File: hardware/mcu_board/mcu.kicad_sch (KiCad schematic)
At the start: 21 parts, among them J1 TEMP, J4 DISPLAY, J4 LEDS_IN, J7 RTC, SW1 RESET, SW1 RotaryEncoder_Switch, U1 ESP32-S3-DevKitC, U2 TOP, U3 BOTTOM, U4 COLD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

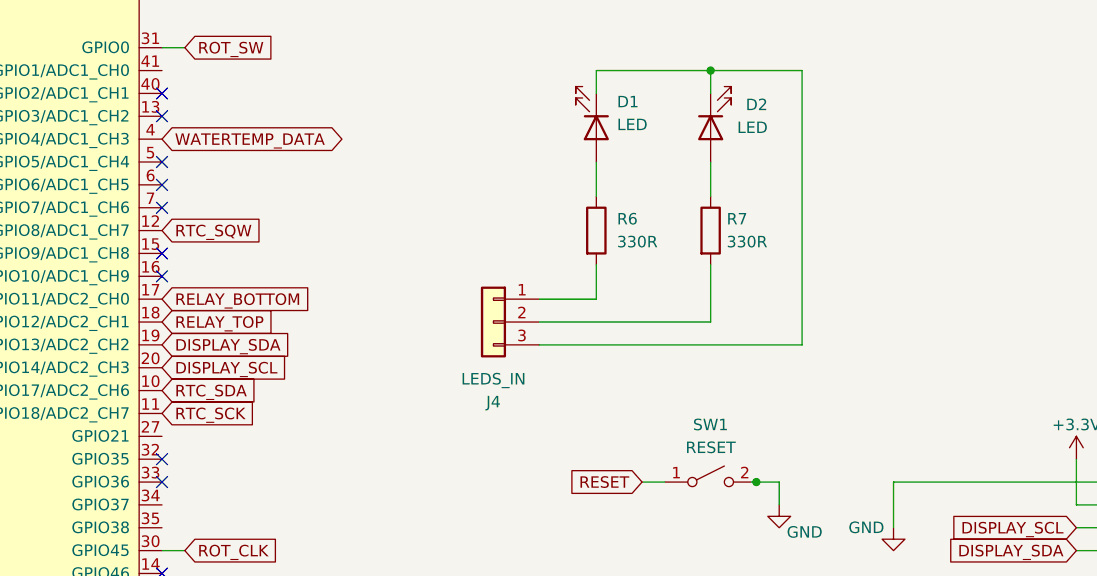
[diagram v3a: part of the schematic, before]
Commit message: fix boards so they components are on the correct side lol
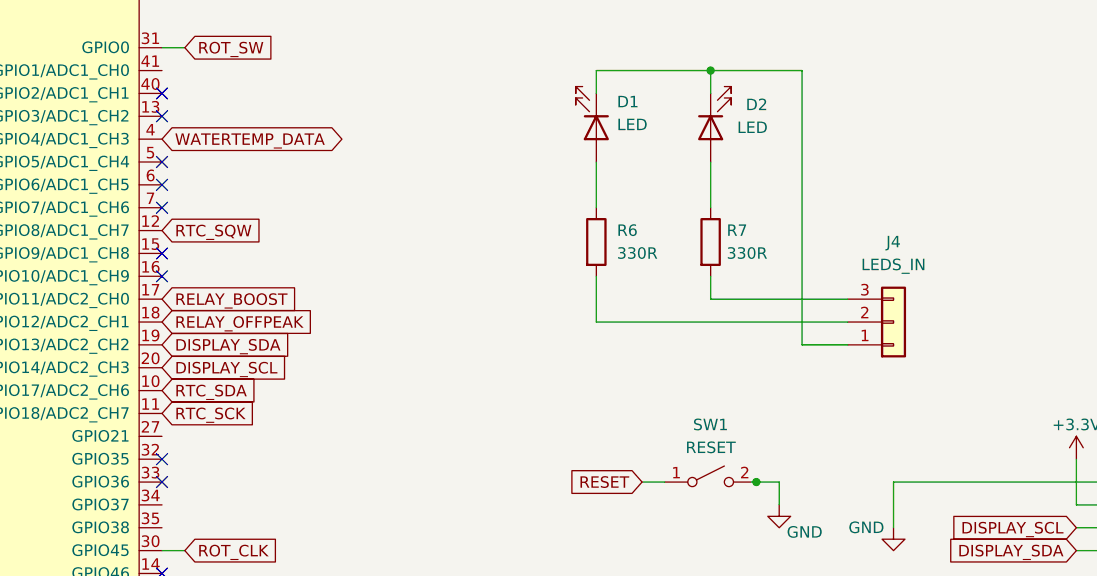
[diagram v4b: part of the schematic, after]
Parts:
- J1: footprint Connector_Audio_2:Jack_3.5mm_PJ320D_Horizontal -> Connector_Audio:Jack_3.5mm_PJ320D_Horizontal
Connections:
- net at D1.1 (K), D2.1 (K): now also J4.1 (Pin_1); no longer J4.3 (Pin_3)
- net at R6.2: now also J4.2 (Pin_2); no longer J4.1 (Pin_1)
- net at R7.2: now also J4.3 (Pin_3); no longer J4.2 (Pin_2)
- net RELAY_BOTTOM renamed RELAY_BOOST
- net RELAY_TOP renamed RELAY_OFFPEAK
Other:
- moved on the sheet: J4, R6, R7
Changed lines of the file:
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@@
+    (stroke (width 0) (type default))
+  )
+  (wire (pts (xy 165.1 81.28) (xy 165.1 83.82))
     (stroke (width 0) (type default))
   )
@@
     (stroke (width 0) (type default))
   )
-  (wire (pts (xy 165.1 68.58) (xy 165.1 72.39))
+  (wire (pts (xy 165.1 68.58) (xy 165.1 73.66))
     (stroke (width 0) (type default))
   )
@@
     (stroke (width 0) (type default))
   )
-  (wire (pts (xy 146.05 88.9) (xy 175.26 88.9))
-    (stroke (width 0) (type default))
-  )
-  (wire (pts (xy 152.4 80.01) (xy 152.4 83.82))
+  (wire (pts (xy 152.4 81.28) (xy 152.4 86.36))
     (stroke (width 0) (type default))
   )
@@
     (stroke (width 0) (type default))
   )
-  (wire (pts (xy 146.05 83.82) (xy 152.4 83.82))
-    (stroke (width 0) (type default))
-  )
   (wire (pts (xy 139.7 40.64) (xy 139.7 43.18))
     (stroke (width 0) (type default))
@@
     (stroke (width 0) (type default))
   )
-  (wire (pts (xy 146.05 86.36) (xy 165.1 86.36))
-    (stroke (width 0) (type default))
-  )
   (wire (pts (xy 205.74 101.6) (xy 205.74 106.68))
     (stroke (width 0) (type default))
@@
     (stroke (width 0) (type default))
   )
+  (wire (pts (xy 165.1 83.82) (xy 180.34 83.82))
+    (stroke (width 0) (type default))
+  )
   (wire (pts (xy 169.672 104.14) (xy 170.18 104.14))
     (stroke (width 0) (type default))
@@
     (stroke (width 0) (type default))
   )
-  (wire (pts (xy 152.4 68.58) (xy 152.4 72.39))
+  (wire (pts (xy 152.4 68.58) (xy 152.4 73.66))
     (stroke (width 0) (type default))
   )
@@
     (stroke (width 0) (type default))
   )
-  (wire (pts (xy 165.1 86.36) (xy 165.1 80.01))
-    (stroke (width 0) (type default))
-  )
   (wire (pts (xy 258.318 65.278) (xy 258.318 61.976))
     (stroke (width 0) (type default))
@@
     (stroke (width 0) (type default))
   )
+  (wire (pts (xy 180.34 86.36) (xy 152.4 86.36))
+    (stroke (width 0) (type default))
+  )
   (wire (pts (xy 262.128 50.546) (xy 253.746 50.546))
     (stroke (width 0) (type default))
@@
   )
   (wire (pts (xy 157.48 137.16) (xy 180.34 137.16))
+    (stroke (width 0) (type default))
+  )
+  (wire (pts (xy 175.26 88.9) (xy 180.34 88.9))
     (stroke (width 0) (type default))
   )
@@
     )
   )
-  (global_label "RELAY_BOTTOM" (shape input) (at 104.14 83.82 0) (fields_autoplaced)
-    (effects (font (size 1.27 1.27)) (justify left))
-    (property "Intersheetrefs" "${INTERSHEET_REFS}" (at 120.9553 83.82 0)
+  (global_label "RELAY_BOOST" (shape input) (at 104.14 83.82 0) (fields_autoplaced)
+    (effects (font (size 1.27 1.27)) (justify left))
+    (property "Intersheetrefs" "${INTERSHEET_REFS}" (at 119.8252 83.82 0)
       (effects (font (size 1.27 1.27)) (justify left) hide)
     )
@@
     )
   )
-  (global_label "RELAY_TOP" (shape input) (at 104.14 86.36 0) (fields_autoplaced)
-    (effects (font (size 1.27 1.27)) (justify left))
-    (property "Intersheetrefs" "${INTERSHEET_REFS}" (at 117.2058 86.36 0)
+  (global_label "RELAY_OFFPEAK" (shape input) (at 104.14 86.36 0) (fields_autoplaced)
+    (effects (font (size 1.27 1.27)) (justify left))
+    (property "Intersheetrefs" "${INTERSHEET_REFS}" (at 122.0024 86.36 0)
       (effects (font (size 1.27 1.27)) (justify left) hide)
     )
@@
       (effects (font (size 1.27 1.27)))
     )
-    (property "Footprint" "Connector_Audio_2:Jack_3.5mm_PJ320D_Horizontal" (at 175.26 33.02 0)
+    (property "Footprint" "Connector_Audio:Jack_3.5mm_PJ320D_Horizontal" (at 175.26 33.02 0)
       (effects (font (size 1.27 1.27)) hide)
     )
@@
     )
   )
-  (symbol (lib_id "Connector_Generic:Conn_01x03") (at 140.97 86.36 0) (mirror y) (unit 1)
-    (in_bom yes) (on_board yes) (dnp no)
-    (property "Reference" "J4" (at 140.97 95.25 0)
-      (effects (font (size 1.27 1.27)))
-    )
-    (property "Value" "LEDS_IN" (at 140.97 92.71 0)
-      (effects (font (size 1.27 1.27)))
-    )
-    (property "Footprint" "Connector_PinHeader_2.54mm:PinHeader_1x03_P2.54mm_Vertical" (at 140.97 86.36 0)
-      (effects (font (size 1.27 1.27)) hide)
-    )
-    (property "Datasheet" "~" (at 140.97 86.36 0)
+  (symbol (lib_id "Connector_Generic:Conn_01x03") (at 185.42 86.36 0) (mirror x) (unit 1)
+    (in_bom yes) (on_board yes) (dnp no)
+    (property "Reference" "J4" (at 185.42 77.47 0)
+      (effects (font (size 1.27 1.27)))
+    )
+    (property "Value" "LEDS_IN" (at 185.42 80.01 0)
+      (effects (font (size 1.27 1.27)))
+    )
+    (property "Footprint" "Connector_PinHeader_2.54mm:PinHeader_1x03_P2.54mm_Vertical" (at 185.42 86.36 0)
+      (effects (font (size 1.27 1.27)) hide)
+    )
+    (property "Datasheet" "~" (at 185.42 86.36 0)
       (effects (font (size 1.27 1.27)) hide)
     )
@@
     )
   )
-  (symbol (lib_id "Device:R") (at 152.4 76.2 0) (unit 1)
+  (symbol (lib_id "Device:R") (at 152.4 77.47 0) (unit 1)
     (in_bom yes) (on_board yes) (dnp no) (fields_autoplaced)
-    (property "Reference" "R6" (at 154.686 74.93 0)
-      (effects (font (size 1.27 1.27)) (justify left))
-    )
-    (property "Value" "330R" (at 154.686 77.47 0)
-      (effects (font (size 1.27 1.27)) (justify left))
-    )
-    (property "Footprint" "Resistor_SMD:R_0805_2012Metric_Pad1.20x1.40mm_HandSolder" (at 150.622 76.2 90)
-      (effects (font (size 1.27 1.27)) hide)
-    )
-    (property "Datasheet" "~" (at 152.4 76.2 0)
+    (property "Reference" "R6" (at 154.686 76.2 0)
+      (effects (font (size 1.27 1.27)) (justify left))
+    )
+    (property "Value" "330R" (at 154.686 78.74 0)
+      (effects (font (size 1.27 1.27)) (justify left))
+    )
+    (property "Footprint" "Resistor_SMD:R_0805_2012Metric_Pad1.20x1.40mm_HandSolder" (at 150.622 77.47 90)
+      (effects (font (size 1.27 1.27)) hide)
+    )
+    (property "Datasheet" "~" (at 152.4 77.47 0)
       (effects (font (size 1.27 1.27)) hide)
     )
@@
     )
   )
-  (symbol (lib_id "Device:R") (at 165.1 76.2 0) (unit 1)
+  (symbol (lib_id "Device:R") (at 165.1 77.47 0) (unit 1)
     (in_bom yes) (on_board yes) (dnp no) (fields_autoplaced)
-    (property "Reference" "R7" (at 166.878 74.93 0)
-      (effects (font (size 1.27 1.27)) (justify left))
-    )
-    (property "Value" "330R" (at 166.878 77.47 0)
-      (effects (font (size 1.27 1.27)) (justify left))
-    )
-    (property "Footprint" "Resistor_SMD:R_0805_2012Metric_Pad1.20x1.40mm_HandSolder" (at 163.322 76.2 90)
-      (effects (font (size 1.27 1.27)) hide)
-    )
-    (property "Datasheet" "~" (at 165.1 76.2 0)
-      (effects (font (size 1.27 1.27)) hide)
-    )
+    (property "Reference" "R7" (at 166.878 76.2 0)
+      (effects (font (size 1.27 1.27)) (justify left))
+    )
+    (property "Value" "330R" (at 166.878 78.74 0)
+      (effects (font (size 1.27 1.27)) (justify left))
+    )
+    (property "Footprint" "Resistor_SMD:R_0805_2012Metric_Pad1.20x1.40mm_HandSolder" (at 163.322 77.47 90)
+      (effects (font (size 1.27 1.27)) hide)
+    )
+    (property "Datasheet" "~" (at 165.1 77.47 0)
+      (effects (font (size 1.27 1.27)) hide)
+    )

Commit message: minor tweaks
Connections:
- net ROT_SW: now also U1.16 (GPIO10/ADC1_CH9); no longer U1.31 (GPIO0)
- no-connect marks 22 -> 31
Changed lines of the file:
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@@
   (junction (at 240.284 74.93) (diameter 0) (color 0 0 0 0)
   )
+  (no_connect (at 104.14 116.84))
   (no_connect (at 53.34 58.42))
   (no_connect (at 258.826 97.028))
+  (no_connect (at 104.14 45.72))
   (no_connect (at 104.14 63.5))
+  (no_connect (at 104.14 99.06))
   (no_connect (at 104.14 60.96))
   (no_connect (at 53.34 60.96))
+  (no_connect (at 53.34 45.72))
   (no_connect (at 53.34 55.88))
+  (no_connect (at 104.14 48.26))
   (no_connect (at 104.14 73.66))
   (no_connect (at 104.14 101.6))
   (no_connect (at 104.14 104.14))
-  (no_connect (at 104.14 81.28))
+  (no_connect (at 104.14 58.42))
   (no_connect (at 104.14 38.1))
   (no_connect (at 53.34 63.5))
@@
   (no_connect (at 258.826 94.488))
   (no_connect (at 104.14 78.74))
+  (no_connect (at 104.14 55.88))
   (no_connect (at 104.14 71.12))
+  (no_connect (at 104.14 109.22))
   (no_connect (at 104.14 40.64))
+  (no_connect (at 104.14 106.68))
   (no_connect (at 104.14 114.3))
   (no_connect (at 78.74 33.02))
   (no_connect (at 104.14 68.58))
+  (no_connect (at 53.34 48.26))
   (no_connect (at 258.826 99.568))
   (wire (pts (xy 152.4 121.92) (xy 175.26 121.92))
@@
     (stroke (width 0) (type default))
   )
+  (wire (pts (xy 104.14 81.28) (xy 106.68 81.28))
+    (stroke (width 0) (type default))
+  )
   (wire (pts (xy 232.664 65.278) (xy 227.33 65.278))
     (stroke (width 0) (type default))
@@
     (stroke (width 0) (type default))
   )
-  (wire (pts (xy 104.14 55.88) (xy 106.68 55.88))
-    (stroke (width 0) (type default))
-  )
   (wire (pts (xy 273.812 46.99) (xy 253.746 46.99))
     (stroke (width 0) (type default))
@@
     )
   )
-  (global_label "ROT_SW" (shape input) (at 106.68 55.88 0) (fields_autoplaced)
-    (effects (font (size 1.27 1.27)) (justify left))
-    (property "Intersheetrefs" "${INTERSHEET_REFS}" (at 116.7824 55.88 0)
-      (effects (font (size 1.27 1.27)) (justify left) hide)
-    )
+  (global_label "ROT_SW" (shape input) (at 106.68 81.28 0) (fields_autoplaced)
+    (effects (font (size 1.27 1.27)) (justify left))
+    (property "Intersheetrefs" "${INTERSHEET_REFS}" (at 116.7824 81.28 0)
+      (effects (font (size 1.27 1.27)) (justify left) hide)
+    )

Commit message: v3 first draft
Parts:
- D1: value LED -> LED_BT
- D2: value LED -> LED_OP
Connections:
- net ROT_CLK: now also U1.28 (GPIO47); no longer U1.30 (GPIO45)
- net ROT_DT: now also U1.27 (GPIO21); no longer U1.29 (GPIO48)
- net ROT_SW: now also U1.15 (GPIO9/ADC1_CH8); no longer U1.16 (GPIO10/ADC1_CH9)
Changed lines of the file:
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@@
   (junction (at 240.284 74.93) (diameter 0) (color 0 0 0 0)
   )
-  (no_connect (at 104.14 116.84))
+  (no_connect (at 53.34 55.88))
   (no_connect (at 53.34 58.42))
   (no_connect (at 258.826 97.028))
   (no_connect (at 104.14 45.72))
   (no_connect (at 104.14 63.5))
-  (no_connect (at 104.14 99.06))
   (no_connect (at 104.14 60.96))
   (no_connect (at 53.34 60.96))
   (no_connect (at 53.34 45.72))
-  (no_connect (at 53.34 55.88))
+  (no_connect (at 104.14 81.28))
+  (no_connect (at 104.14 109.22))
   (no_connect (at 104.14 48.26))
   (no_connect (at 104.14 73.66))
@@
   (no_connect (at 104.14 38.1))
   (no_connect (at 53.34 63.5))
+  (no_connect (at 104.14 119.38))
   (no_connect (at 180.34 35.56))
   (no_connect (at 258.826 102.108))
   (no_connect (at 258.826 94.488))
-  (no_connect (at 104.14 78.74))
   (no_connect (at 104.14 55.88))
+  (no_connect (at 104.14 111.76))
   (no_connect (at 104.14 71.12))
-  (no_connect (at 104.14 109.22))
   (no_connect (at 104.14 40.64))
   (no_connect (at 104.14 106.68))
@@
     (stroke (width 0) (type default))
   )
-  (wire (pts (xy 104.14 119.38) (xy 106.68 119.38))
-    (stroke (width 0) (type default))
-  )
   (wire (pts (xy 157.48 137.16) (xy 157.48 144.78))
     (stroke (width 0) (type default))
@@
     (stroke (width 0) (type default))
   )
+  (wire (pts (xy 104.14 78.74) (xy 106.68 78.74))
+    (stroke (width 0) (type default))
+  )
   (wire (pts (xy 165.1 68.58) (xy 165.1 73.66))
     (stroke (width 0) (type default))
@@
     (stroke (width 0) (type default))
   )
-  (wire (pts (xy 104.14 111.76) (xy 106.68 111.76))
-    (stroke (width 0) (type default))
-  )
   (wire (pts (xy 170.18 134.62) (xy 175.26 134.62))
     (stroke (width 0) (type default))
@@
     (stroke (width 0) (type default))
   )
-  (wire (pts (xy 104.14 81.28) (xy 106.68 81.28))
-    (stroke (width 0) (type default))
-  )
   (wire (pts (xy 232.664 65.278) (xy 227.33 65.278))
     (stroke (width 0) (type default))
@@
     (stroke (width 0) (type default))
   )
+  (wire (pts (xy 104.14 99.06) (xy 106.68 99.06))
+    (stroke (width 0) (type default))
+  )
   (wire (pts (xy 234.95 46.99) (xy 253.746 46.99))
     (stroke (width 0) (type default))
@@
   )
   (wire (pts (xy 78.74 127) (xy 78.74 121.92))
+    (stroke (width 0) (type default))
+  )
+  (wire (pts (xy 104.14 116.84) (xy 106.68 116.84))
     (stroke (width 0) (type default))
   )
@@
     )
   )
-  (global_label "ROT_SW" (shape input) (at 106.68 81.28 0) (fields_autoplaced)
-    (effects (font (size 1.27 1.27)) (justify left))
-    (property "Intersheetrefs" "${INTERSHEET_REFS}" (at 116.7824 81.28 0)
-      (effects (font (size 1.27 1.27)) (justify left) hide)
-    )
-  )
-  (global_label "ROT_DT" (shape input) (at 106.68 119.38 0) (fields_autoplaced)
-    (effects (font (size 1.27 1.27)) (justify left))
-    (property "Intersheetrefs" "${INTERSHEET_REFS}" (at 116.3591 119.38 0)
+  (global_label "ROT_SW" (shape input) (at 106.68 78.74 0) (fields_autoplaced)
+    (effects (font (size 1.27 1.27)) (justify left))
+    (property "Intersheetrefs" "${INTERSHEET_REFS}" (at 116.7824 78.74 0)
+      (effects (font (size 1.27 1.27)) (justify left) hide)
+    )
+  )
+  (global_label "ROT_DT" (shape input) (at 106.68 99.06 0) (fields_autoplaced)
+    (effects (font (size 1.27 1.27)) (justify left))
+    (property "Intersheetrefs" "${INTERSHEET_REFS}" (at 116.3591 99.06 0)
       (effects (font (size 1.27 1.27)) (justify left) hide)
     )
@@
     )
   )
-  (global_label "ROT_CLK" (shape input) (at 106.68 111.76 0) (fields_autoplaced)
-    (effects (font (size 1.27 1.27)) (justify left))
-    (property "Intersheetrefs" "${INTERSHEET_REFS}" (at 117.6896 111.76 0)
-      (effects (font (size 1.27 1.27)) (justify left) hide)
+  (global_label "ROT_CLK" (shape input) (at 50.8 55.88 180) (fields_autoplaced)
+    (effects (font (size 1.27 1.27)) (justify right))
+    (property "Intersheetrefs" "${INTERSHEET_REFS}" (at 39.711 55.88 0)
+      (effects (font (size 1.27 1.27)) (justify right) hide)
     )
   )
@@
     (effects (font (size 1.27 1.27)) (justify left))
     (property "Intersheetrefs" "${INTERSHEET_REFS}" (at 122.0024 86.36 0)
+      (effects (font (size 1.27 1.27)) (justify left) hide)
+    )
+  )
+  (global_label "ROT_CLK" (shape input) (at 106.68 116.84 0) (fields_autoplaced)
+    (effects (font (size 1.27 1.27)) (justify left))
+    (property "Intersheetrefs" "${INTERSHEET_REFS}" (at 117.769 116.84 0)
       (effects (font (size 1.27 1.27)) (justify left) hide)
     )
@@
   (symbol (lib_id "Device:LED") (at 152.4 64.77 270) (unit 1)
     (in_bom yes) (on_board yes) (dnp no) (fields_autoplaced)
-    (property "Reference" "D1" (at 154.686 61.9125 90)
+    (property "Reference" "D1" (at 154.94 61.9125 90)
       (effects (font (size 1.27 1.27)) (justify left))
     )
-    (property "Value" "LED" (at 154.686 64.4525 90)
+    (property "Value" "LED_BT" (at 154.94 64.4525 90)
       (effects (font (size 1.27 1.27)) (justify left))
     )
@@
       (effects (font (size 1.27 1.27)) (justify left))
     )
-    (property "Value" "LED" (at 171.45 64.77 90)
+    (property "Value" "LED_OP" (at 173.736 64.77 90)
       (effects (font (size 1.27 1.27)) (justify left))
     )
